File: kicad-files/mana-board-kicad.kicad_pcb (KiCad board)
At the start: 2 copper layers, 155.5 x 110 mm, 44 parts, among them U1 Pico

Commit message: Organize libraries, start rev1
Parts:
- removed REF** (x5): MountingHole_2.2mm_M2, MountingHole:MountingHole_2.2mm_M2
- B1, B2, B3, B4, DOWN1, L1, L2, LEFT1, R1, R2, RIGHT1, UP1: footprint Switch_Keyboard_Kailh:SW_Kailh_Choc_V2_1.00u -> ManaBoard:SW_Kailh_Choc_V2
- D1: value SK6812MINI -> SK6812MINI-E; footprint Footprints:SK6812-MINI-E-reversed -> ManaBoard:SK6812-MINI-E
- D10, D11, D12, D2, D3, D4, D5, D6, D7, D8, D9: footprint Footprints:SK6812-MINI-E-reversed -> ManaBoard:SK6812-MINI-E
- R4, R5: value R_Small -> 5.1k
- TP2: value TestPoint -> PI DM
- TP3: value TestPoint -> PI DP
- moved S1 92.0 mm to (139.3, 125.5)
- moved S2 92.0 mm to (151.5, 125.5)
- moved D12 45.4 mm to (234.2, 72.8), turned to -150 degrees
- moved L2 43.1 mm to (231.8, 68.5), turned to 30 degrees
- moved D8 37.5 mm to (224.2, 55.4), turned to -150 degrees
- moved A2 36.5 mm to (135.8, 43.8)
- moved A1 36.5 mm to (148.0, 43.8)
- moved D11 35.9 mm to (211.1, 82.7), turned to -150 degrees
- moved L1 35.4 mm to (221.8, 51.2), turned to 30 degrees
- moved TP2 34.5 mm to (233.3, 136.2)
- moved TP3 34.5 mm to (233.3, 134.2)
- moved TP6 34.5 mm to (221.5, 132.8)
- moved U1 34.5 mm to (209.2, 135.2)
- moved R2 33.5 mm to (208.6, 78.4), turned to 30 degrees
- moved D9 29.2 mm to (172.3, 115.5), turned to -150 degrees
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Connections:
- D1 pad 1: Net-(D1-DOUT) -> 5V
- D1 pad 2: GND -> Net-(D1-DOUT)
- D1 pad 3: Net-(D1-DIN) -> GND
- D1 pad 4: Net-(D1-VDD) -> RGBDATA
- D10 pad 1: Net-(D10-DOUT) -> 5V
- D10 pad 2: GND -> Net-(D10-DOUT)
- D10 pad 3: Net-(D10-DIN) -> GND
- D10 pad 4: Net-(D1-VDD) -> Net-(D10-DIN)
- D11 pad 1: Net-(D11-DOUT) -> 5V
- D11 pad 2: GND -> Net-(D11-DOUT)
- D11 pad 3: Net-(D10-DOUT) -> GND
- D11 pad 4: Net-(D1-VDD) -> Net-(D10-DOUT)
- D12 pad 1: unconnected-(D12-DOUT-Pad1) -> 5V
- D12 pad 2: GND -> unconnected-(D12-DOUT-Pad2)
- D12 pad 3: Net-(D11-DOUT) -> GND
- D12 pad 4: Net-(D1-VDD) -> Net-(D11-DOUT)
- D2 pad 1: Net-(D2-DOUT) -> 5V
- D2 pad 2: GND -> Net-(D2-DOUT)
- D2 pad 3: Net-(D1-DOUT) -> GND
- D2 pad 4: Net-(D1-VDD) -> Net-(D1-DOUT)
- D3 pad 1: Net-(D3-DOUT) -> 5V
- D3 pad 2: GND -> Net-(D3-DOUT)
- D3 pad 3: Net-(D2-DOUT) -> GND
- D3 pad 4: Net-(D1-VDD) -> Net-(D2-DOUT)
- D4 pad 1: Net-(D4-DOUT) -> 5V
- D4 pad 2: GND -> Net-(D4-DOUT)
- D4 pad 3: Net-(D3-DOUT) -> GND
- D4 pad 4: Net-(D1-VDD) -> Net-(D3-DOUT)
- D5 pad 1: Net-(D5-DOUT) -> 5V
- D5 pad 2: GND -> Net-(D5-DOUT)
- D5 pad 3: Net-(D4-DOUT) -> GND
- D5 pad 4: Net-(D1-VDD) -> Net-(D4-DOUT)
- D6 pad 1: Net-(D6-DOUT) -> 5V
- D6 pad 2: GND -> Net-(D6-DOUT)
- D6 pad 3: Net-(D5-DOUT) -> GND
- D6 pad 4: Net-(D1-VDD) -> Net-(D5-DOUT)
- D7 pad 1: Net-(D7-DOUT) -> 5V
- D7 pad 2: GND -> Net-(D7-DOUT)
- D7 pad 3: Net-(D6-DOUT) -> GND
- D7 pad 4: Net-(D1-VDD) -> Net-(D6-DOUT)
- D8 pad 1: Net-(D8-DOUT) -> 5V
- D8 pad 2: GND -> Net-(D8-DOUT)
- D8 pad 3: Net-(D7-DOUT) -> GND
- D8 pad 4: Net-(D1-VDD) -> Net-(D7-DOUT)
- D9 pad 1: Net-(D10-DIN) -> 5V
- D9 pad 2: GND -> Net-(D10-DIN)
- D9 pad 3: Net-(D8-DOUT) -> GND
- D9 pad 4: Net-(D1-VDD) -> Net-(D8-DOUT)
- U1 pad 28: GND -> unconnected-(U1-GND-Pad28)
- U1 pad 34: Net-(D1-DIN) -> RGBDATA
- U1 pad 36: Net-(D1-VDD) -> 3.3V
- U1 pad 40: Net-(U1-VBUS) -> 5V
- USB1 pad A4: Net-(U1-VBUS) -> 5V
- USB1 pad A9: Net-(U1-VBUS) -> 5V
- USB1 pad B4: Net-(U1-VBUS) -> 5V
- USB1 pad B9: Net-(U1-VBUS) -> 5V
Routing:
- net Net-(D1-VDD): track 639.6 -> 0.00 mm
- net Net-(U1-GPIO21): track 296.1 -> 0.00 mm
- net Net-(U1-GPIO20): track 278.1 -> 0.00 mm
- net Net-(U1-GPIO19): track 248.6 -> 0.00 mm
- net Net-(U1-GPIO18): track 232.0 -> 0.00 mm
- net Net-(U1-GPIO17): track 188.6 -> 0.00 mm
- net Net-(D2-DOUT): track 171.3 -> 0.00 mm
- net Net-(U1-GPIO16): track 171.1 -> 0.00 mm
- net Net-(U1-VBUS): track 154.8 -> 0.00 mm, vias 2 -> 0
- net Net-(U1-GPIO5): track 150.9 -> 0.00 mm
- net Net-(D1-DOUT): track 144.3 -> 0.00 mm
- net Net-(U1-GPIO13): track 141.5 -> 0.00 mm
- net Net-(D1-DIN): track 139.2 -> 0.00 mm
- net /Pi D-: track 141.0 -> 7.18 mm
- net /Pi D+: track 139.1 -> 7.54 mm
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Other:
- board size 155.5 x 110 mm -> 200 x 125 mm

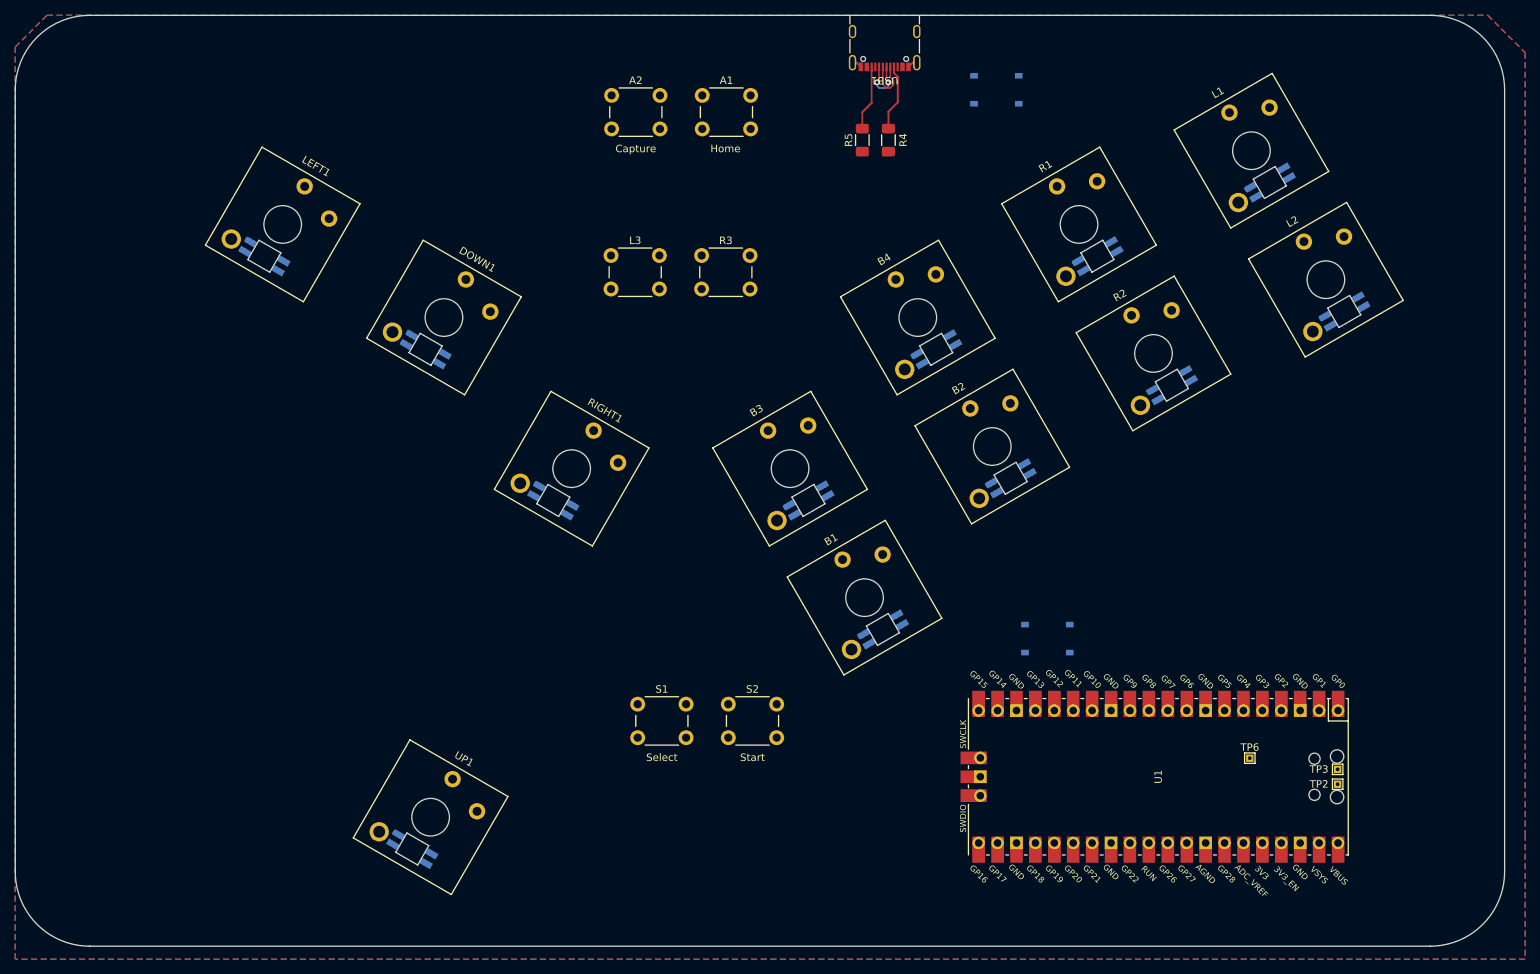
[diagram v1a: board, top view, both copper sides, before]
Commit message: First pass at wiring rev1
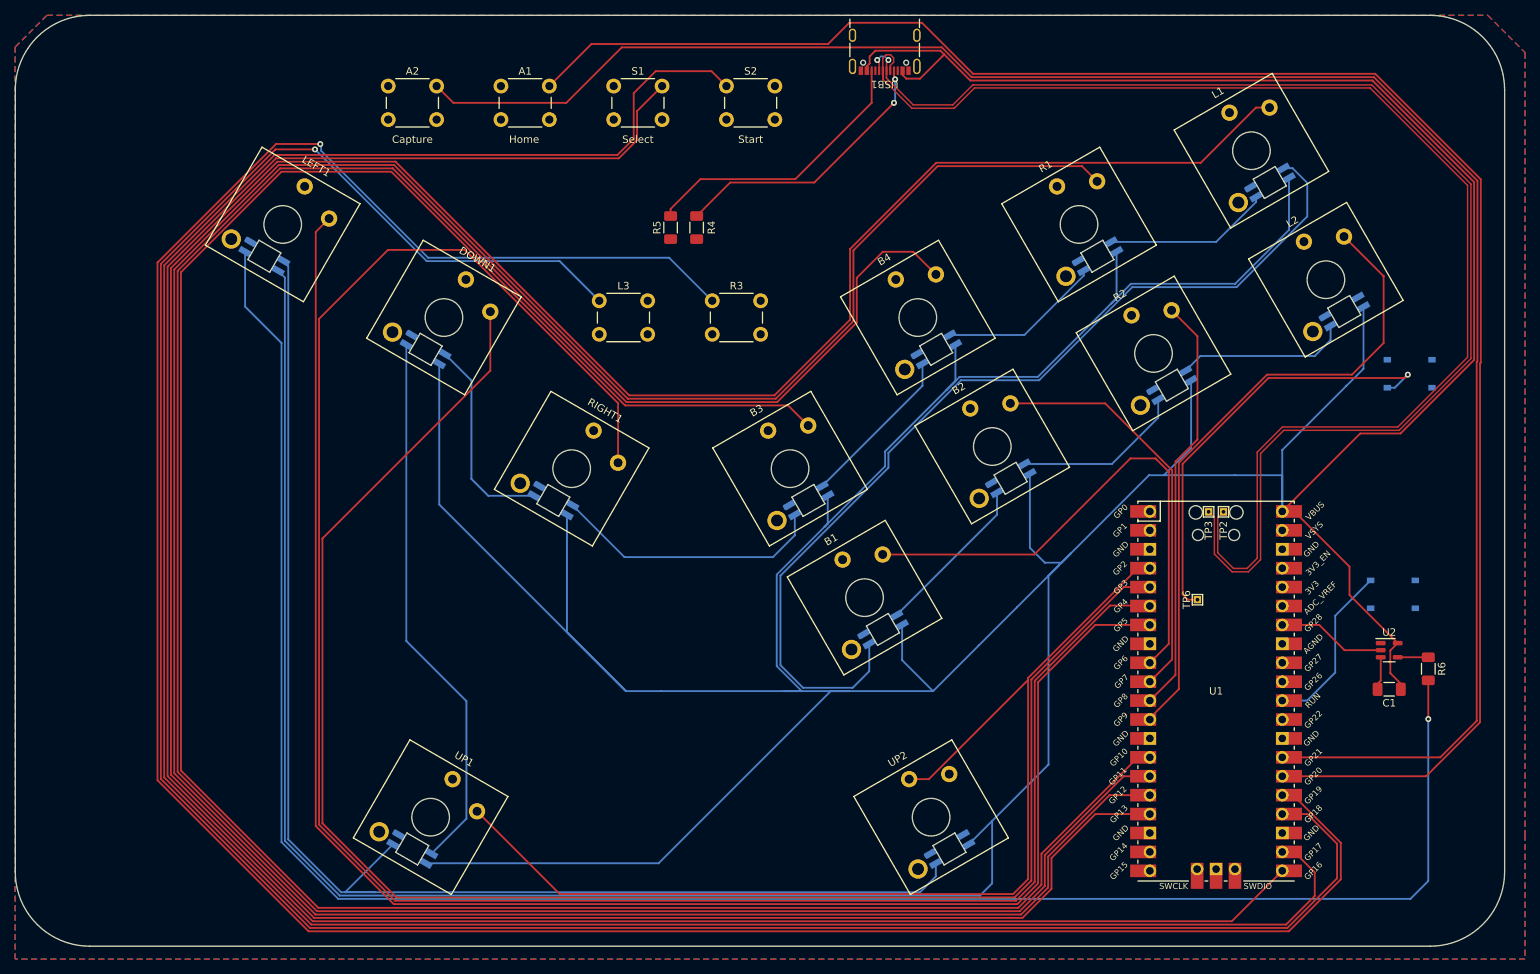
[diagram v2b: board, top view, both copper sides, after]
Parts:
- added C1: 100nF, Capacitor_SMD:C_1206_3216Metric_Pad1.33x1.80mm_HandSolder, F.Cu at (240.2, 123.5)
- added D13: SK6812MINI-E, ManaBoard:SK6812-MINI-E, B.Cu at (181.2, 144.9)
- added R6: 10k, Resistor_SMD:R_1206_3216Metric_Pad1.30x1.75mm_HandSolder, F.Cu at (245.5, 120.8)
- added U2: 74AHCT1G125, Package_TO_SOT_SMD:SOT-23-5, F.Cu at (240.2, 118.2)
- added UP2: SW_Push, ManaBoard:SW_Kailh_Choc_V2, F.Cu at (178.7, 140.7)
- U1: footprint MCU_RaspberryPi_and_Boards:RPi_Pico_SMD_TH -> ManaBoard:RPi_Pico_SMD_TH
- moved S1 83.1 mm to (136.1, 42.5)
- moved S2 83.0 mm to (151.2, 42.5)
- moved BOOTSEL1 67.3 mm to (243.0, 81.1)
- moved RESET1 46.8 mm to (240.8, 110.8)
- moved TP2 39.7 mm to (218.0, 99.7), turned to -90 degrees
- moved TP3 38.7 mm to (216.0, 99.7), turned to -90 degrees
- moved A2 30.0 mm to (105.8, 42.5)
- moved R4 28.3 mm to (147.2, 61.5)
- moved R5 28.3 mm to (143.8, 61.5)
- moved A1 27.1 mm to (121.0, 42.5)
- moved TP6 22.4 mm to (214.5, 111.5), turned to 90 degrees
- moved U1 13.9 mm to (217.0, 123.8), turned to 0 degrees
- moved L3 6.28 mm to (134.2, 71.3)
- moved R3 6.25 mm to (149.3, 71.3)
- moved USB1 0.50 mm to (172.5, 36.8)
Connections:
- D1 pad 4: RGBDATA -> RGBDATA_5V
- U1 pad 28: unconnected-(U1-GND-Pad28) -> GND
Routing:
- net 5V: track 0.00 -> 874.7 mm
- net Net-(U1-GPIO13): track 0.00 -> 403.7 mm
- net Net-(U1-GPIO12): track 0.00 -> 377.7 mm
- net Net-(U1-GPIO11): track 0.00 -> 349.2 mm
- net Net-(U1-GPIO19): track 0.00 -> 345.4 mm, vias 0 -> 1
- net Net-(U1-GPIO17): track 0.00 -> 332.4 mm
- net Net-(U1-GPIO18): track 0.00 -> 325.5 mm, vias 0 -> 1
- net Net-(U1-GPIO10): track 0.00 -> 319.4 mm
- net Net-(U1-GPIO16): track 0.00 -> 307.7 mm
- net Net-(U1-GPIO4): track 0.00 -> 276.5 mm
- net RGBDATA_5V: track 0.00 -> 266.4 mm, vias 0 -> 1
- net Net-(U1-GPIO21): track 0.00 -> 251.9 mm
- net Net-(U1-GPIO20): track 0.00 -> 239.8 mm
- net Net-(U1-GPIO5): track 0.00 -> 230.0 mm
- net Net-(U1-GPIO3): track 0.00 -> 226.4 mm
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
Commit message: update board a little
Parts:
- added C10: 100nF, Capacitor_SMD:C_1206_3216Metric_Pad1.33x1.80mm_HandSolder, B.Cu at (174.3, 118.9)
- added C11: 100nF, Capacitor_SMD:C_1206_3216Metric_Pad1.33x1.80mm_HandSolder, B.Cu at (191.4, 98.6)
- added C12: 100nF, Capacitor_SMD:C_1206_3216Metric_Pad1.33x1.80mm_HandSolder, B.Cu at (213.1, 86.1)
- added C13: 100nF, Capacitor_SMD:C_1206_3216Metric_Pad1.33x1.80mm_HandSolder, B.Cu at (236.2, 76.2)
- added C14: 100nF, Capacitor_SMD:C_1206_3216Metric_Pad1.33x1.80mm_HandSolder, B.Cu at (183.2, 148.4)
- added C2: 100nF, Capacitor_SMD:C_1206_3216Metric_Pad1.33x1.80mm_HandSolder, B.Cu at (87.2, 68.8)
- added C3: 100nF, Capacitor_SMD:C_1206_3216Metric_Pad1.33x1.80mm_HandSolder, B.Cu at (107.1, 148.4)
- added C4: 100nF, Capacitor_SMD:C_1206_3216Metric_Pad1.33x1.80mm_HandSolder, B.Cu at (108.8, 81.3)
- added C5: 100nF, Capacitor_SMD:C_1206_3216Metric_Pad1.33x1.80mm_HandSolder, B.Cu at (126.0, 101.6)
- added C6: 100nF, Capacitor_SMD:C_1206_3216Metric_Pad1.33x1.80mm_HandSolder, B.Cu at (164.3, 101.6)
- added C7: 100nF, Capacitor_SMD:C_1206_3216Metric_Pad1.33x1.80mm_HandSolder, B.Cu at (181.4, 81.3)
- added C8: 100nF, Capacitor_SMD:C_1206_3216Metric_Pad1.33x1.80mm_HandSolder, B.Cu at (203.1, 68.8)
- added C9: 100nF, Capacitor_SMD:C_1206_3216Metric_Pad1.33x1.80mm_HandSolder, B.Cu at (226.2, 58.9)
- added REF**: MountingHole_2.1mm, MountingHole:MountingHole_2.1mm, F.Cu at (188.8, 109.8)
- added REF**: MountingHole_2.1mm, MountingHole:MountingHole_2.1mm, F.Cu at (65.8, 43.0)
- added REF**: MountingHole_2.1mm, MountingHole:MountingHole_2.1mm, F.Cu at (245.8, 43.0)
- added REF**: MountingHole_2.1mm, MountingHole:MountingHole_2.1mm, F.Cu at (145.2, 99.8)
- added REF**: MountingHole_2.1mm, MountingHole:MountingHole_2.1mm, F.Cu at (245.8, 148.0)
- added REF**: MountingHole_2.1mm, MountingHole:MountingHole_2.1mm, F.Cu at (65.8, 148.0)
- U1: footprint ManaBoard:RPi_Pico_SMD_TH -> MCU_RaspberryPi_and_Boards:RPi_Pico_SMD_TH
- moved BOOTSEL1 15.0 mm to (240.8, 96.0)
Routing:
- net Net-(BOOTSEL1-Pad2): track 58.5 -> 32.2 mm, vias 1 -> 0
- net 5V: track 874.7 -> 882.6 mm
- net GND: track 3.73 -> 6.44 mm, vias 0 -> 13
- net Net-(D2-DOUT): track 73.6 -> 76.1 mm
- net Net-(U1-GPIO13): track 403.7 -> 401.7 mm
- net Net-(U1-GPIO12): track 377.7 -> 375.7 mm
- net Net-(D8-DOUT): track 130.2 -> 128.6 mm

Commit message: rev1 sent for prototyping
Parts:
- REF** (x6): footprint MountingHole:MountingHole_2.1mm -> ManaBoard:MountingHole_2.1mm
- moved R3 69.5 mm to (153.4, 140.7)
- moved L3 69.4 mm to (136.9, 140.7)
- moved R5 41.2 mm to (183.0, 49.0), turned to 180 degrees
- moved R4 39.2 mm to (183.0, 45.5), turned to 180 degrees
- moved REF** 20.0 mm to (125.2, 99.8)
- moved REF** 10.3 mm to (186.2, 99.7)
- moved D8 9.08 mm to (230.0, 62.4)
- moved C9 9.08 mm to (232.0, 65.9)
- moved L1 9.08 mm to (227.5, 58.2)
- moved C13 9.08 mm to (242.0, 83.2)
- moved D12 9.08 mm to (240.0, 79.8)
- moved L2 9.08 mm to (237.5, 75.5)
- moved C5 8.99 mm to (123.1, 93.1)
- moved D4 8.99 mm to (125.1, 89.6)
- moved RIGHT1 8.99 mm to (127.5, 85.4)
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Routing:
- net Net-(U1-GPIO19): track 345.4 -> 79.1 mm
- net Net-(U1-GPIO18): track 325.5 -> 97.7 mm
- net 5V: track 882.6 -> 940.3 mm, vias 0 -> 1
- net Net-(U1-GPIO3): track 226.4 -> 265.1 mm
- net Net-(U1-GPIO2): track 150.4 -> 119.2 mm
- net Net-(U1-GPIO16): track 307.7 -> 337.1 mm
- net Net-(USB1-CC1): track 37.2 -> 10.7 mm
- net Net-(D2-DOUT): track 76.1 -> 102.5 mm
- net Net-(U1-GPIO17): track 332.4 -> 353.4 mm
- net Net-(USB1-CC2): track 38.2 -> 17.7 mm
- net Net-(U1-GPIO4): track 276.5 -> 295.8 mm
- net Net-(U1-GPIO10): track 319.4 -> 338.6 mm
- net Net-(U1-GPIO5): track 230.0 -> 244.6 mm
- net Net-(U1-GPIO21): track 251.9 -> 261.7 mm
- net Net-(U1-GPIO6): track 71.2 -> 62.6 mm
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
